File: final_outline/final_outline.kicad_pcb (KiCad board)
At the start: 2 copper layers, 99.5 x 75 mm, 24 parts, among them P001 CANCONNECTOR, P002 AUXCONNECTOR, P100 ISP, P101 DEBUG_LED, U401 ISO1050, U403 LPC11C14, U501 MCP1755

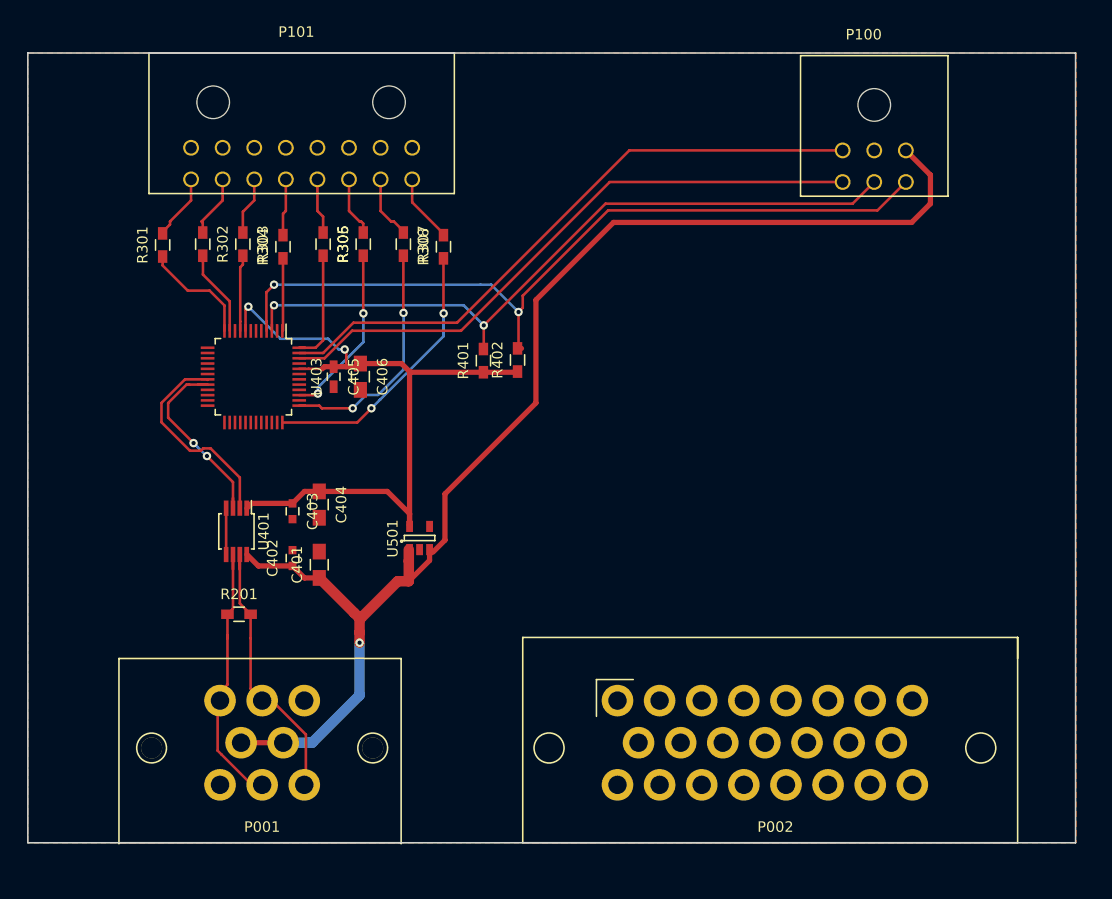
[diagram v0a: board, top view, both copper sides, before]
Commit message: Added gnd planes
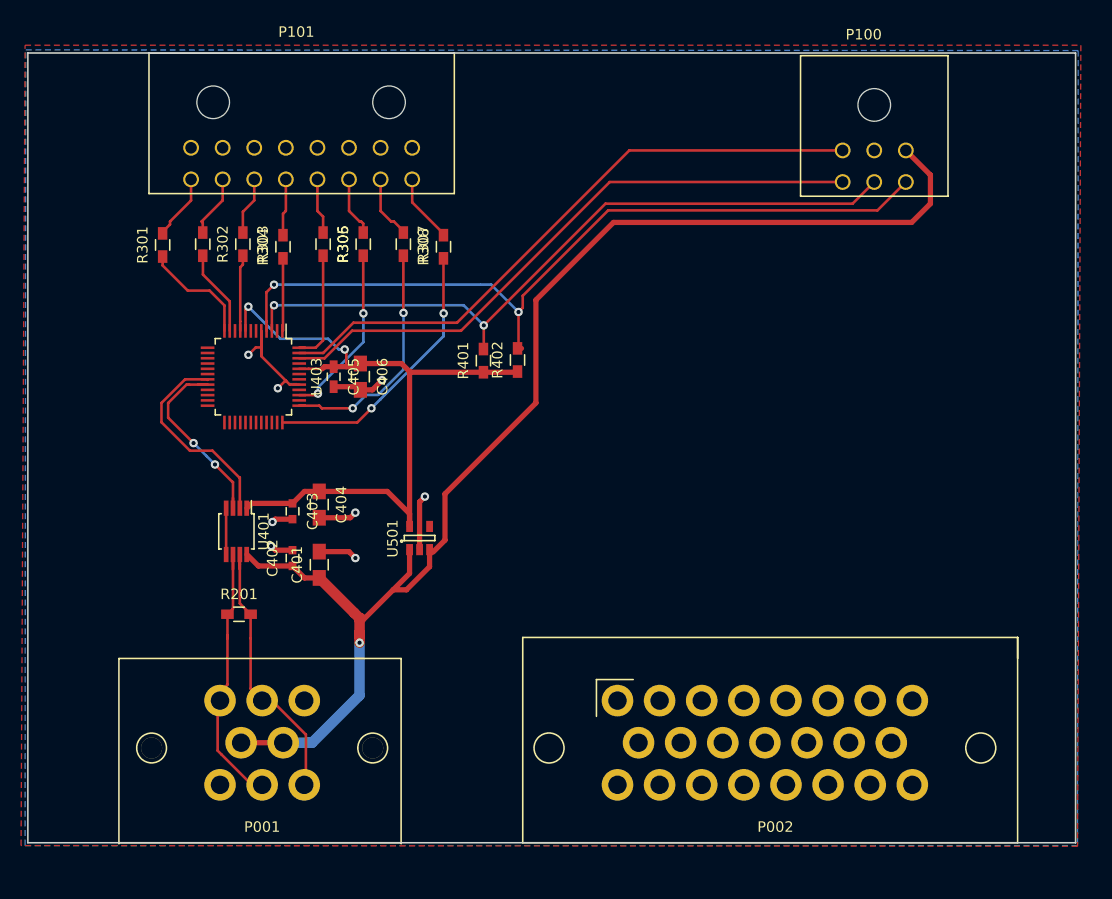
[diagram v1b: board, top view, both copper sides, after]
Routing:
- net GND: track 4.82 -> 39.1 mm, vias 0 -> 8
- net +5V: track 122.1 -> 124.1 mm
- added copper zone on B.Cu, net GND

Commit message: 12V added
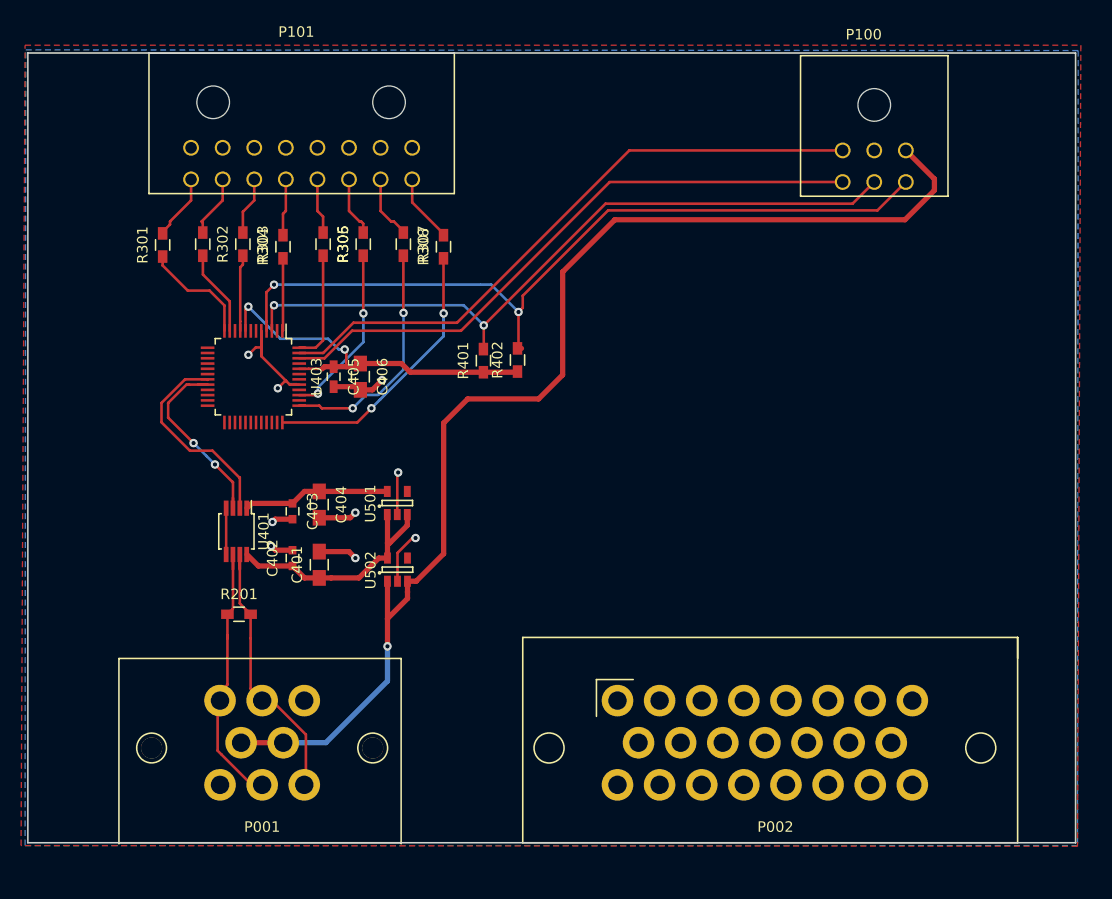
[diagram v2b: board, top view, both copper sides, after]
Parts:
- added U502: MCP1755-5, Housings_SOT-23_SOT-143_TSOT-6:SOT-23-5, F.Cu at (137.6, 102.1)
- U501: value MCP1755 -> MCP1755-33
- moved U501 3.94 mm to (137.6, 95.7)
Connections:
- P001 pad 4: +5V -> +12V
- P001 pad 5: +5V -> +12V
- P100 pad 3: +5V -> +12V
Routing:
- net +12V: track 0.00 -> 113.5 mm, vias 0 -> 1
- net +5V: track 124.1 -> 22.8 mm, vias 1 -> 0
- net +3V3: track 69.4 -> 50.3 mm
- net GND: track 39.1 -> 42.3 mm, vias 8 -> 9
- net (no net): track 0.00 -> 0.63 mm

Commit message: updated final outline, added capacitors, switched CAN chip
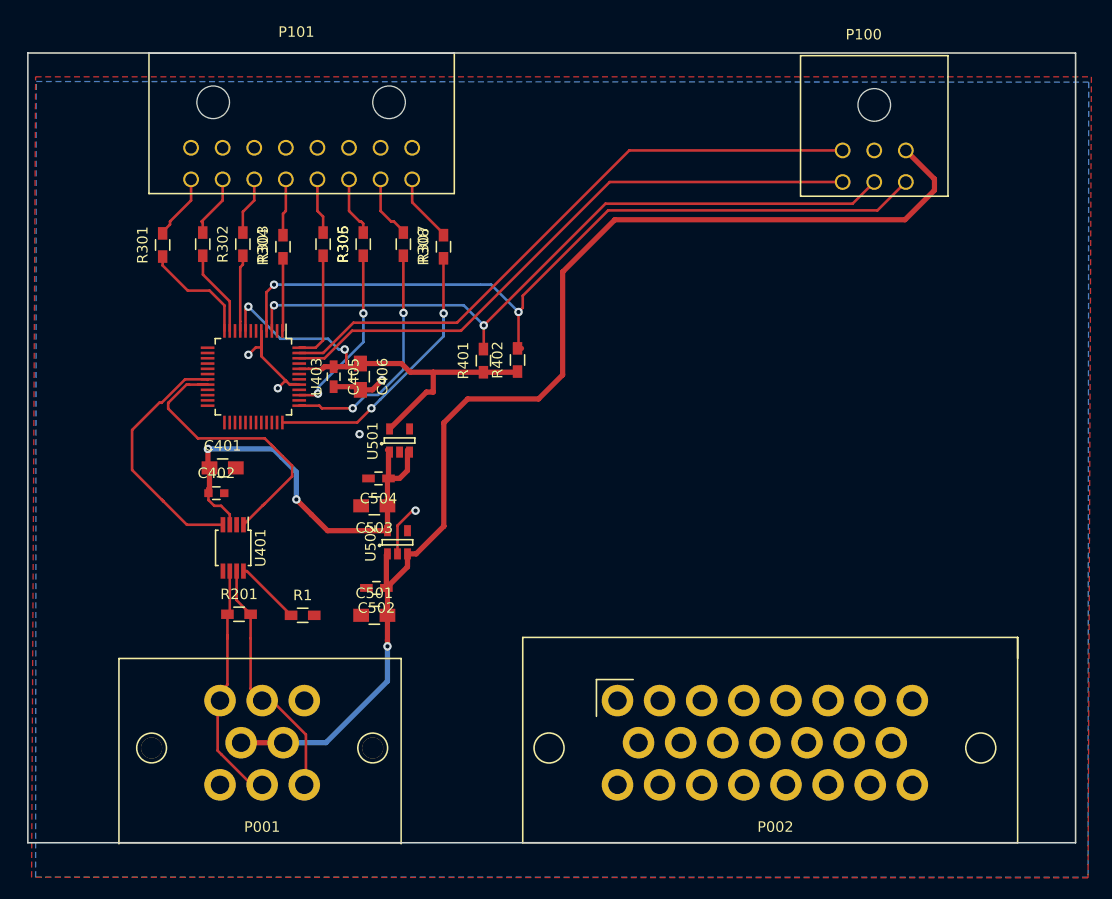
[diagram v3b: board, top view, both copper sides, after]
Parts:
- removed C403: 0.1uF, Capacitors_SMD:C_0603
- removed C404: 10uF, Capacitors_SMD:C_0805_HandSoldering
- added C501: 10μ, Capacitors_SMD:C_0805_HandSoldering, F.Cu at (135.4, 106.4)
- added C502: .1μ, Capacitors_SMD:C_0603_HandSoldering, F.Cu at (135.6, 103.8)
- added C503: 10μ, Capacitors_SMD:C_0805_HandSoldering, F.Cu at (135.4, 96.0)
- added C504: .1μ, Capacitors_SMD:C_0603_HandSoldering, F.Cu at (135.8, 93.4)
- added R1: 20k, Resistors_SMD:R_0603_HandSoldering, F.Cu at (128.6, 106.4)
- U401: value ISO1050 -> MCP2551-I/SN
- moved C401 13.0 mm to (121.0, 92.4), turned to 0 degrees
- moved C402 9.51 mm to (120.4, 94.8), turned to 0 degrees
- moved U501 5.94 mm to (137.8, 89.8)
- moved U502 2.60 mm to (137.6, 99.5)
- moved U401 1.60 mm to (122.0, 100.0)
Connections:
- U401 pad 1: +3V3 -> /Micro_Controller/CAN_TXD
- U401 pad 2: /Micro_Controller/CAN_RXD -> GND
- U401 pad 3: /Micro_Controller/CAN_TXD -> +5V
- U401 pad 4: GND -> /Micro_Controller/CAN_RXD
- U401 pad 5: GND -> Net-(U401-Pad5)
- U401 pad 8: +5V -> Net-(R1-Pad1)
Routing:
- net GND: track 42.3 -> 22.2 mm, vias 9 -> 4
- net +5V: track 22.8 -> 42.0 mm, vias 0 -> 2
- net /Micro_Controller/CAN_TXD: track 19.0 -> 28.1 mm, vias 2 -> 0
- net +3V3: track 50.3 -> 43.8 mm
- net Net-(R1-Pad1): track 0.00 -> 6.26 mm
- net /Micro_Controller/CAN_RXD: track 19.8 -> 24.2 mm
- net /BACK_PANEL/CANL: track 26.4 -> 23.3 mm
- net /BACK_PANEL/CANH: track 26.1 -> 23.2 mm
- net (no net): track 0.63 -> 0.89 mm, vias 0 -> 1
